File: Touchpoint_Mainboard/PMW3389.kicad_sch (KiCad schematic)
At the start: 14 parts, among them U1 PMW3360DM, U3 TLS105B0MBHTSA1

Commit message: Finished assigning most footprints
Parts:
- C19, C23, C26: footprint (none) -> Capacitor_SMD:C_0805_2012Metric
- C20, C21, C22, C24, C25, C27: footprint (none) -> Capacitor_SMD:C_0402_1005Metric
- R11, R12, R13: footprint (none) -> Resistor_SMD:R_0402_1005Metric
- U3: footprint PG-SCT-595-5_INF -> Touchpoint:PG-SCT-595-5_INF
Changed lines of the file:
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@@
 			)
 		)
-		(property "Footprint" ""
+		(property "Footprint" "Resistor_SMD:R_0402_1005Metric"
 			(at 50.038 59.69 90)
 			(effects
@@
 			)
 		)
-		(property "Footprint" ""
+		(property "Footprint" "Resistor_SMD:R_0402_1005Metric"
 			(at 85.852 29.21 90)
 			(effects
@@
 			)
 		)
-		(property "Footprint" ""
+		(property "Footprint" "Capacitor_SMD:C_0402_1005Metric"
 			(at 97.4852 33.02 0)
 			(effects
@@
 			)
 		)
-		(property "Footprint" ""
+		(property "Footprint" "Capacitor_SMD:C_0402_1005Metric"
 			(at 178.7652 41.91 0)
 			(effects
@@
 			)
 		)
-		(property "Footprint" ""
+		(property "Footprint" "Capacitor_SMD:C_0402_1005Metric"
 			(at 28.9052 33.02 0)
 			(effects
@@
 			)
 		)
-		(property "Footprint" ""
+		(property "Footprint" "Capacitor_SMD:C_0402_1005Metric"
 			(at 28.9052 53.34 0)
 			(effects
@@
 			)
 		)
-		(property "Footprint" ""
+		(property "Footprint" "Capacitor_SMD:C_0805_2012Metric"
 			(at 107.6452 33.02 0)
 			(effects
@@
 			)
 		)
-		(property "Footprint" ""
+		(property "Footprint" "Resistor_SMD:R_0402_1005Metric"
 			(at 88.392 44.45 90)
 			(effects
@@
 			)
 		)
-		(property "Footprint" ""
+		(property "Footprint" "Capacitor_SMD:C_0805_2012Metric"
 			(at 17.4752 53.34 0)
 			(effects
@@
 			)
 		)
-		(property "Footprint" ""
+		(property "Footprint" "Capacitor_SMD:C_0805_2012Metric"
 			(at 17.4752 76.2 0)
 			(effects
@@
 			)
 		)
-		(property "Footprint" ""
+		(property "Footprint" "Capacitor_SMD:C_0402_1005Metric"
 			(at 28.9052 76.2 0)
 			(effects
@@
 			)
 		)
-		(property "Footprint" "PG-SCT-595-5_INF"
+		(property "Footprint" "Touchpoint:PG-SCT-595-5_INF"
 			(at 127 29.21 0)
 			(effects
@@
 			)
 		)
-		(property "Footprint" ""
+		(property "Footprint" "Capacitor_SMD:C_0402_1005Metric"
 			(at 17.4752 33.02 0)
 			(effects

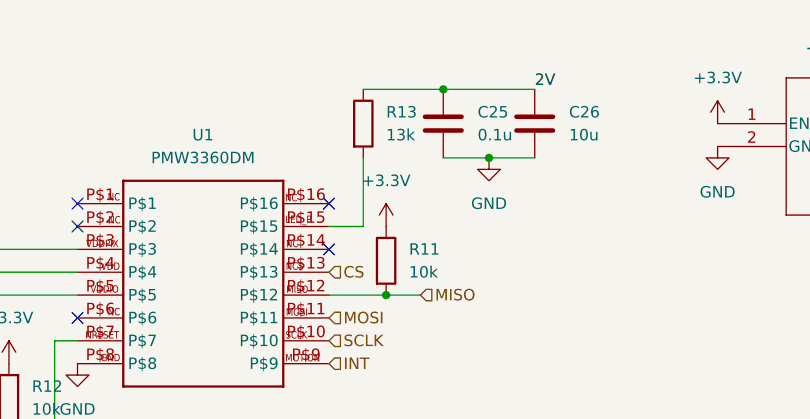
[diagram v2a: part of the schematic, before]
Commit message: Changed some component values based on availability
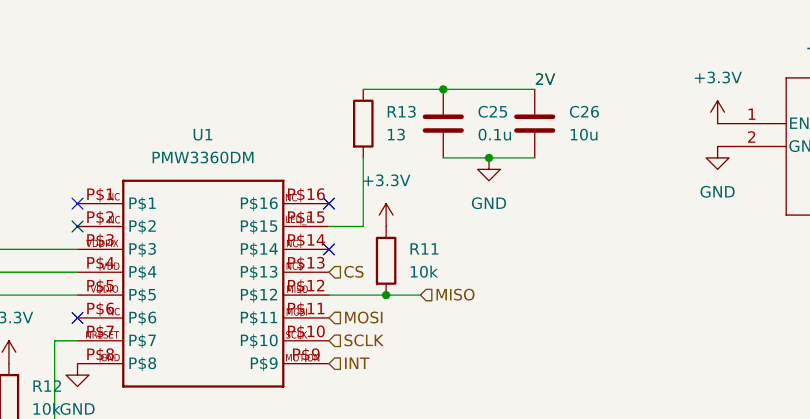
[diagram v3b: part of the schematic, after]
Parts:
- R13: value 13k -> 13
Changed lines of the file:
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@@
 			)
 		)
-		(property "Value" "13k"
+		(property "Value" "13"
 			(at 90.17 30.4799 0)
 			(effects

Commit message: Finished assigning footprints and 3d models for both boards
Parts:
- U1: footprint =Custom:PMW3360DM -> Touchpoint:PMW3360DM
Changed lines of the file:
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@@
 			)
 		)
-		(property "Footprint" "=Custom:PMW3360DM"
+		(property "Footprint" "Touchpoint:PMW3360DM"
 			(at 59.69 60.96 0)
 			(effects

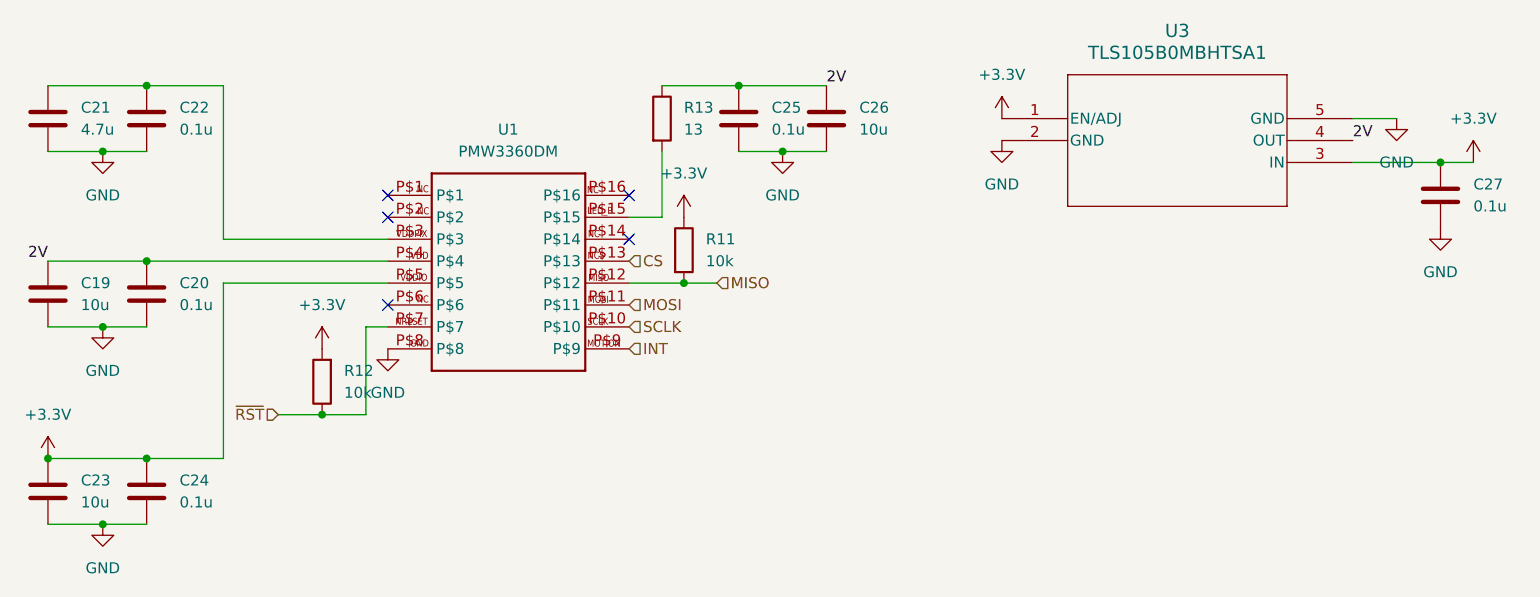
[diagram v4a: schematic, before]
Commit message: Added 3.3V to interface
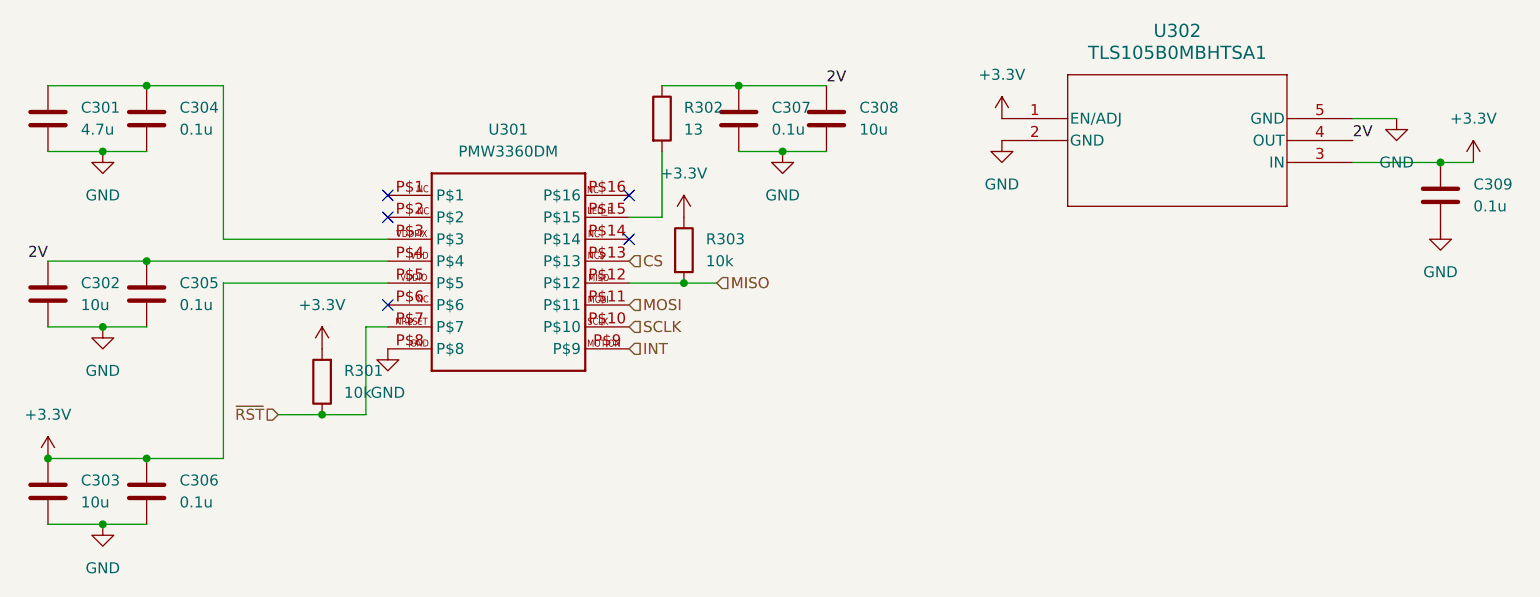
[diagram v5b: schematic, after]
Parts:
- renumbered C21 to C301, C19 to C302, C23 to C303, C22 to C304, C20 to C305, C24 to C306, C25 to C307, C26 to C308, C27 to C309, R12 to R301, R13 to R302, R11 to R303, U1 to U301, U3 to U302
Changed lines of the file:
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@@
 		(dnp no)
 		(fields_autoplaced yes)
-		(property "Reference" "R12"
+		(property "Reference" "R301"
 			(at 50.8 58.4199 0)
 			(effects
@@
 			(project ""
 				(path "/f37b5f88-420a-4646-85df-8f9851d23e3c/091850a6-fc48-4da5-acfb-c3187b00b1b9"
-					(reference "R12")
+					(reference "R301")
 					(unit 1)
 				)
@@
 		(dnp no)
 		(fields_autoplaced yes)
-		(property "Reference" "R13"
+		(property "Reference" "R302"
 			(at 90.17 27.9399 0)
 			(effects
@@
 			(project ""
 				(path "/f37b5f88-420a-4646-85df-8f9851d23e3c/091850a6-fc48-4da5-acfb-c3187b00b1b9"
-					(reference "R13")
+					(reference "R302")
 					(unit 1)
 				)
@@
 		(dnp no)
 		(fields_autoplaced yes)
-		(property "Reference" "C25"
+		(property "Reference" "C307"
 			(at 100.33 27.9399 0)
 			(effects
@@
 			(project ""
 				(path "/f37b5f88-420a-4646-85df-8f9851d23e3c/091850a6-fc48-4da5-acfb-c3187b00b1b9"
-					(reference "C25")
+					(reference "C307")
 					(unit 1)
 				)
@@
 		(dnp no)
 		(fields_autoplaced yes)
-		(property "Reference" "C27"
+		(property "Reference" "C309"
 			(at 181.61 36.8299 0)
 			(effects
@@
 			(project "Touchpoint_Mainboard"
 				(path "/f37b5f88-420a-4646-85df-8f9851d23e3c/091850a6-fc48-4da5-acfb-c3187b00b1b9"
-					(reference "C27")
+					(reference "C309")
 					(unit 1)
 				)
@@
 		(dnp no)
 		(fields_autoplaced yes)
-		(property "Reference" "#PWR029"
+		(property "Reference" "#PWR0301"
 			(at 16.51 72.39 0)
 			(effects
@@
 			(project ""
 				(path "/f37b5f88-420a-4646-85df-8f9851d23e3c/091850a6-fc48-4da5-acfb-c3187b00b1b9"
-					(reference "#PWR029")
+					(reference "#PWR0301")
 					(unit 1)
 				)
@@
 		(dnp no)
 		(fields_autoplaced yes)
-		(property "Reference" "#PWR032"
+		(property "Reference" "#PWR0307"
 			(at 90.17 44.45 0)
 			(effects
@@
 			(project ""
 				(path "/f37b5f88-420a-4646-85df-8f9851d23e3c/091850a6-fc48-4da5-acfb-c3187b00b1b9"
-					(reference "#PWR032")
+					(reference "#PWR0307")
 					(unit 1)
 				)
@@
 		(dnp no)
 		(fields_autoplaced yes)
-		(property "Reference" "C22"
+		(property "Reference" "C304"
 			(at 31.75 27.9399 0)
 			(effects
@@
 			(project "Touchpoint_Mainboard"
 				(path "/f37b5f88-420a-4646-85df-8f9851d23e3c/091850a6-fc48-4da5-acfb-c3187b00b1b9"
-					(reference "C22")
+					(reference "C304")
 					(unit 1)
 				)
@@
 		(dnp no)
 		(fields_autoplaced yes)
-		(property "Reference" "#PWR026"
+		(property "Reference" "#PWR0303"
 			(at 22.86 59.69 0)
 			(effects
@@
 			(project ""
 				(path "/f37b5f88-420a-4646-85df-8f9851d23e3c/091850a6-fc48-4da5-acfb-c3187b00b1b9"
-					(reference "#PWR026")
+					(reference "#PWR0303")
 					(unit 1)
 				)
@@
 		(dnp no)
 		(fields_autoplaced yes)
-		(property "Reference" "#PWR039"
+		(property "Reference" "#PWR0313"
 			(at 181.61 38.1 0)
 			(effects
@@
 			(project "Touchpoint_Mainboard"
 				(path "/f37b5f88-420a-4646-85df-8f9851d23e3c/091850a6-fc48-4da5-acfb-c3187b00b1b9"
-					(reference "#PWR039")
+					(reference "#PWR0313")
 					(unit 1)
 				)
@@
 		(dnp no)
 		(fields_autoplaced yes)
-		(property "Reference" "C20"
+		(property "Reference" "C305"
 			(at 31.75 48.2599 0)
 			(effects
@@
 			(project "Touchpoint_Mainboard"
 				(path "/f37b5f88-420a-4646-85df-8f9851d23e3c/091850a6-fc48-4da5-acfb-c3187b00b1b9"
-					(reference "C20")
+					(reference "C305")
 					(unit 1)
 				)
@@
 		(dnp no)
 		(fields_autoplaced yes)
-		(property "Reference" "C26"
+		(property "Reference" "C308"
 			(at 110.49 27.9399 0)
 			(effects
@@
 			(project "Touchpoint_Mainboard"
 				(path "/f37b5f88-420a-4646-85df-8f9851d23e3c/091850a6-fc48-4da5-acfb-c3187b00b1b9"
-					(reference "C26")
+					(reference "C308")
 					(unit 1)
 				)
@@
 		(dnp no)
 		(fields_autoplaced yes)
-		(property "Reference" "#PWR034"
+		(property "Reference" "#PWR0308"
 			(at 101.6 39.37 0)
 			(effects
@@
 			(project "Touchpoint_Mainboard"
 				(path "/f37b5f88-420a-4646-85df-8f9851d23e3c/091850a6-fc48-4da5-acfb-c3187b00b1b9"
-					(reference "#PWR034")
+					(reference "#PWR0308")
 					(unit 1)
 				)
@@
 		(dnp no)
 		(fields_autoplaced yes)
-		(property "Reference" "#PWR027"
+		(property "Reference" "#PWR0302"
 			(at 22.86 39.37 0)
 			(effects
@@
 			(project ""
 				(path "/f37b5f88-420a-4646-85df-8f9851d23e3c/091850a6-fc48-4da5-acfb-c3187b00b1b9"
-					(reference "#PWR027")
+					(reference "#PWR0302")
 					(unit 1)
 				)
@@
 		(dnp no)
 		(fields_autoplaced yes)
-		(property "Reference" "R11"
+		(property "Reference" "R303"
 			(at 92.71 43.1799 0)
 			(effects
@@
 			(project ""
 				(path "/f37b5f88-420a-4646-85df-8f9851d23e3c/091850a6-fc48-4da5-acfb-c3187b00b1b9"
-					(reference "R11")
+					(reference "R303")
 					(unit 1)
 				)
@@
 		(dnp no)
 		(fields_autoplaced yes)
-		(property "Reference" "#PWR037"
+		(property "Reference" "#PWR0310"
 			(at 127 38.1 0)
 			(effects
@@
 			(project "Touchpoint_Mainboard"
 				(path "/f37b5f88-420a-4646-85df-8f9851d23e3c/091850a6-fc48-4da5-acfb-c3187b00b1b9"
-					(reference "#PWR037")
+					(reference "#PWR0310")
 					(unit 1)
 				)
@@
 		(dnp no)
 		(fields_autoplaced yes)
-		(property "Reference" "C19"
+		(property "Reference" "C302"
 			(at 20.32 48.2599 0)
 			(effects
@@
 			(project ""
 				(path "/f37b5f88-420a-4646-85df-8f9851d23e3c/091850a6-fc48-4da5-acfb-c3187b00b1b9"
-					(reference "C19")
+					(reference "C302")
 					(unit 1)
 				)
@@
 		(dnp no)
 		(fields_autoplaced yes)
-		(property "Reference" "#PWR031"
+		(property "Reference" "#PWR0306"
 			(at 55.88 62.23 0)
 			(effects
@@
 			(project ""
 				(path "/f37b5f88-420a-4646-85df-8f9851d23e3c/091850a6-fc48-4da5-acfb-c3187b00b1b9"
-					(reference "#PWR031")
+					(reference "#PWR0306")
 					(unit 1)
 				)
@@
 		(dnp no)
 		(fields_autoplaced yes)
-		(property "Reference" "C23"
+		(property "Reference" "C303"
 			(at 20.32 71.1199 0)
 			(effects
@@
 			(project "Touchpoint_Mainboard"
 				(path "/f37b5f88-420a-4646-85df-8f9851d23e3c/091850a6-fc48-4da5-acfb-c3187b00b1b9"
-					(reference "C23")
+					(reference "C303")
 					(unit 1)
 				)
@@
 		(dnp no)
 		(fields_autoplaced yes)
-		(property "Reference" "#PWR033"
+		(property "Reference" "#PWR0305"
 			(at 48.26 59.69 0)
 			(effects
@@
 			(project "Touchpoint_Mainboard"
 				(path "/f37b5f88-420a-4646-85df-8f9851d23e3c/091850a6-fc48-4da5-acfb-c3187b00b1b9"
-					(reference "#PWR033")
+					(reference "#PWR0305")
 					(unit 1)
 				)
@@
 		(dnp no)
 		(fields_autoplaced yes)
-		(property "Reference" "C24"
+		(property "Reference" "C306"
 			(at 31.75 71.1199 0)
 			(effects
@@
 			(project "Touchpoint_Mainboard"
 				(path "/f37b5f88-420a-4646-85df-8f9851d23e3c/091850a6-fc48-4da5-acfb-c3187b00b1b9"
-					(reference "C24")
+					(reference "C306")
 					(unit 1)
 				)
@@
 		(dnp no)
 		(fields_autoplaced yes)
-		(property "Reference" "U3"
+		(property "Reference" "U302"
 			(at 147.32 19.05 0)
 			(effects
@@
 			(project ""
 				(path "/f37b5f88-420a-4646-85df-8f9851d23e3c/091850a6-fc48-4da5-acfb-c3187b00b1b9"
-					(reference "U3")
+					(reference "U302")
 					(unit 1)
 				)
@@
 		(dnp no)
 		(fields_autoplaced yes)
-		(property "Reference" "C21"
+		(property "Reference" "C301"
 			(at 20.32 27.9399 0)
 			(effects
@@
 			(project "Touchpoint_Mainboard"
 				(path "/f37b5f88-420a-4646-85df-8f9851d23e3c/091850a6-fc48-4da5-acfb-c3187b00b1b9"
-					(reference "C21")
+					(reference "C301")
 					(unit 1)
 				)
@@
 		(dnp no)
 		(fields_autoplaced yes)
-		(property "Reference" "#PWR040"
+		(property "Reference" "#PWR0311"
 			(at 172.72 35.56 0)
 			(effects
@@
 			(project "Touchpoint_Mainboard"
 				(path "/f37b5f88-420a-4646-85df-8f9851d23e3c/091850a6-fc48-4da5-acfb-c3187b00b1b9"
-					(reference "#PWR040")
+					(reference "#PWR0311")
 					(unit 1)
 				)
@@
 		(dnp no)
 		(fields_autoplaced yes)
-		(property "Reference" "#PWR041"
+		(property "Reference" "#PWR0312"
 			(at 177.8 48.26 0)
 			(effects
@@
 			(project "Touchpoint_Mainboard"
 				(path "/f37b5f88-420a-4646-85df-8f9851d23e3c/091850a6-fc48-4da5-acfb-c3187b00b1b9"
-					(reference "#PWR041")
+					(reference "#PWR0312")
 					(unit 1)
 				)
@@
 		(dnp no)
 		(fields_autoplaced yes)
-		(property "Reference" "#PWR038"
+		(property "Reference" "#PWR0309"
 			(at 127 33.02 0)
 			(effects
@@
 			(project "Touchpoint_Mainboard"
 				(path "/f37b5f88-420a-4646-85df-8f9851d23e3c/091850a6-fc48-4da5-acfb-c3187b00b1b9"
-					(reference "#PWR038")
+					(reference "#PWR0309")
 					(unit 1)
 				)
@@
 		(dnp no)
 		(fields_autoplaced yes)
-		(property "Reference" "#PWR030"
+		(property "Reference" "#PWR0304"
 			(at 22.86 82.55 0)
 			(effects
@@
 			(project ""
 				(path "/f37b5f88-420a-4646-85df-8f9851d23e3c/091850a6-fc48-4da5-acfb-c3187b00b1b9"
-					(reference "#PWR030")
+					(reference "#PWR0304")
 					(unit 1)
 				)
@@
 		(dnp no)
 		(fields_autoplaced yes)
-		(property "Reference" "U1"
+		(property "Reference" "U301"
 			(at 69.8229 30.48 0)
 			(effects
@@
 			(project ""
 				(path "/f37b5f88-420a-4646-85df-8f9851d23e3c/091850a6-fc48-4da5-acfb-c3187b00b1b9"
-					(reference "U1")
-					(unit 1)
-				)
+					(reference "U301")
+					(unit 1)
+				)

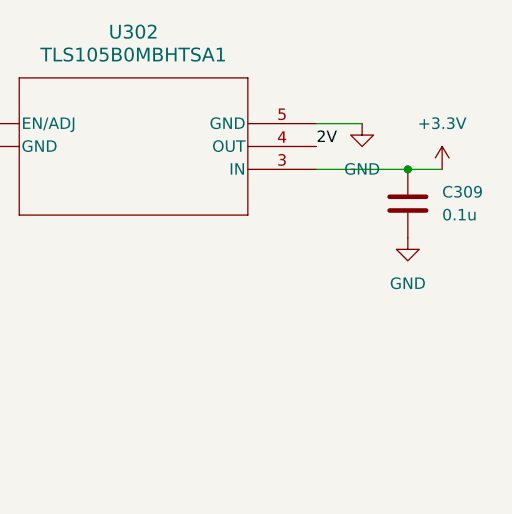
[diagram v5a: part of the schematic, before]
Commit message: Finally finished routing EEOP driver
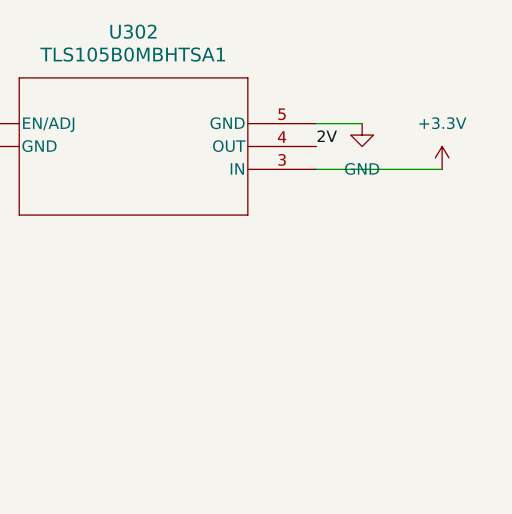
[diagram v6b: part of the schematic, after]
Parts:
- removed C309: 0.1u, Capacitor_SMD:C_0402_1005Metric, symbol Device:C
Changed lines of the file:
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@@
-	)
-	(junction
-		(at 177.8 34.29)
-		(diameter 0)
-		(color 0 0 0 0)
 	)
 	(junction
@@
 	(wire
 		(pts
-			(xy 181.61 34.29) (xy 177.8 34.29)
+			(xy 167.64 34.29) (xy 181.61 34.29)
 		)
 		(stroke
@@
 		(pts
 			(xy 22.86 33.02) (xy 27.94 33.02)
-		)
-		(stroke
-			(width 0)
-			(type default)
-		)
-	)
-	(wire
-		(pts
-			(xy 177.8 34.29) (xy 167.64 34.29)
 		)
 		(stroke
@@
 	)
 	(symbol
-		(lib_id "Device:C")
-		(at 177.8 38.1 0)
-		(unit 1)
-		(exclude_from_sim no)
-		(in_bom yes)
-		(on_board yes)
-		(dnp no)
-		(fields_autoplaced yes)
-		(property "Reference" "C309"
-			(at 181.61 36.8299 0)
-			(effects
-				(font
-					(size 1.27 1.27)
-				)
-				(justify left)
-			)
-		)
-		(property "Value" "0.1u"
-			(at 181.61 39.3699 0)
-			(effects
-				(font
-					(size 1.27 1.27)
-				)
-				(justify left)
-			)
-		)
-		(property "Footprint" "Capacitor_SMD:C_0402_1005Metric"
-			(at 178.7652 41.91 0)
-			(effects
-				(font
-					(size 1.27 1.27)
-				)
-				(hide yes)
-			)
-		)
-		(property "Datasheet" "~"
-			(at 177.8 38.1 0)
-			(effects
-				(font
-					(size 1.27 1.27)
-				)
-				(hide yes)
-			)
-		)
-		(property "Description" "Unpolarized capacitor"
-			(at 177.8 38.1 0)
-			(effects
-				(font
-					(size 1.27 1.27)
-				)
-				(hide yes)
-			)
-		)
-		(pin "2"
-		)
-		(pin "1"
-		)
-		(instances
-			(project "Touchpoint_Mainboard"
-				(path "/f37b5f88-420a-4646-85df-8f9851d23e3c/091850a6-fc48-4da5-acfb-c3187b00b1b9"
-					(reference "C309")
-					(unit 1)
-				)
-			)
-		)
-	)
-	(symbol
 		(lib_id "power:+3.3V")
 		(at 16.51 68.58 0)
@@
 					(unit 1)
 				)
-			)
-		)
-	)
-	(symbol
-		(lib_id "power:GND")
-		(at 177.8 41.91 0)
-		(unit 1)
-		(exclude_from_sim no)
-		(in_bom yes)
-		(on_board yes)
-		(dnp no)
-		(fields_autoplaced yes)
-		(property "Reference" "#PWR0312"
-			(at 177.8 48.26 0)
-			(effects
-				(font
-					(size 1.27 1.27)
-				)
-				(hide yes)
-			)
-		)
-		(property "Value" "GND"
-			(at 177.8 46.99 0)
-			(effects
-				(font
-					(size 1.27 1.27)
-				)
-			)
-		)
-		(property "Footprint" ""
-			(at 177.8 41.91 0)
-			(effects
-				(font
-					(size 1.27 1.27)
-				)
-				(hide yes)
-			)
-		)
-		(property "Datasheet" ""
-			(at 177.8 41.91 0)
-			(effects
-				(font
-					(size 1.27 1.27)
-				)
-				(hide yes)
-			)
-		)
-		(property "Description" "Power symbol creates a global label with name \"GND\" , ground"
-			(at 177.8 41.91 0)
-			(effects
-				(font
-					(size 1.27 1.27)
-				)
-				(hide yes)
-			)
-		)
-		(pin "1"
-		)
-		(instances
-			(project "Touchpoint_Mainboard"
-				(path "/f37b5f88-420a-4646-85df-8f9851d23e3c/091850a6-fc48-4da5-acfb-c3187b00b1b9"
-					(reference "#PWR0312")
-					(unit 1)
-				)
